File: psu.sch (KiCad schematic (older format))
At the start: 4 parts

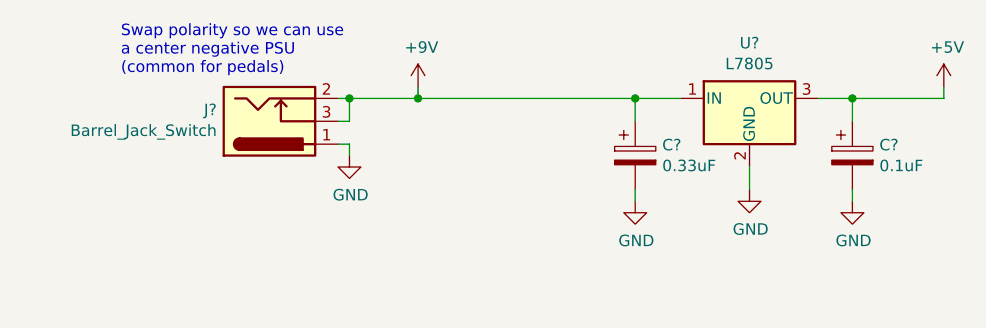
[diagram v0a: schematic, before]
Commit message: Schem entry done, need to do footprints and PCB
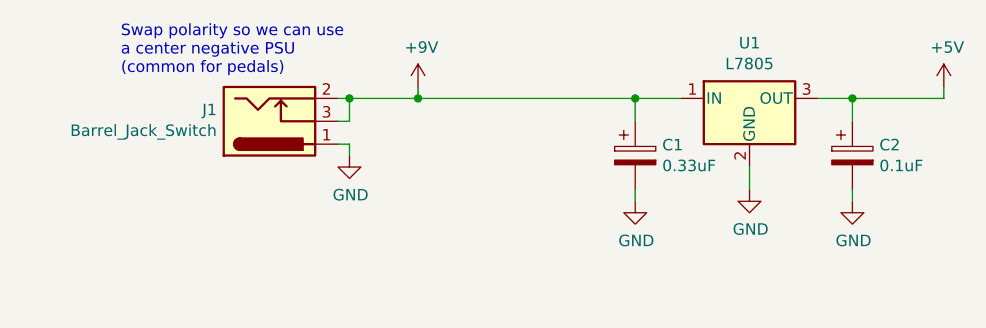
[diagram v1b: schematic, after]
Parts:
- gave numbers to parts that had none: 4
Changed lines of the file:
@@
 EESchema Schematic File Version 4
 LIBS:midi_switcher-cache
-EELAYER 29 0
+EELAYER 30 0
 EELAYER END
 $Descr A4 11693 8268
@@
 $EndDescr
 $Comp
-L Connector:Barrel_Jack_Switch J?
+L Connector:Barrel_Jack_Switch J1
 U 1 1 5D744931
 P 1550 1950
-F 0 "J?" H 1320 1900 50  0000 R CNN
+F 0 "J1" H 1320 1900 50  0000 R CNN
 F 1 "Barrel_Jack_Switch" H 1320 1991 50  0000 R CNN
 F 2 "" H 1600 1910 50  0001 C CNN
@@
 $EndComp
 $Comp
-L power:GND #PWR?
+L power:GND #PWR0101
 U 1 1 5D74594F
 P 1900 2100
-F 0 "#PWR?" H 1900 1850 50  0001 C CNN
+F 0 "#PWR0101" H 1900 1850 50  0001 C CNN
 F 1 "GND" H 1905 1927 50  0000 C CNN
 F 2 "" H 1900 2100 50  0001 C CNN
@@
 	1900 1850 2200 1850
 $Comp
-L power:+9V #PWR?
+L power:+9V #PWR0102
 U 1 1 5D7467A3
 P 2200 1800
-F 0 "#PWR?" H 2200 1650 50  0001 C CNN
+F 0 "#PWR0102" H 2200 1650 50  0001 C CNN
 F 1 "+9V" H 2215 1973 50  0000 C CNN
 F 2 "" H 2200 1800 50  0001 C CNN
@@
 $EndComp
 $Comp
-L Regulator_Linear:L7805 U?
+L Regulator_Linear:L7805 U1
 U 1 1 5D746EA6
 P 3650 1850
-F 0 "U?" H 3650 2092 50  0000 C CNN
+F 0 "U1" H 3650 2092 50  0000 C CNN
 F 1 "L7805" H 3650 2001 50  0000 C CNN
 F 2 "" H 3675 1700 50  0001 L CIN
@@
 $EndComp
 $Comp
-L power:GND #PWR?
+L power:GND #PWR0103
 U 1 1 5D747CA5
 P 3650 2250
-F 0 "#PWR?" H 3650 2000 50  0001 C CNN
+F 0 "#PWR0103" H 3650 2000 50  0001 C CNN
 F 1 "GND" H 3655 2077 50  0000 C CNN
 F 2 "" H 3650 2250 50  0001 C CNN
@@
 	3650 2250 3650 2150
 $Comp
-L Device:CP C?
+L Device:CP C1
 U 1 1 5D748082
 P 3150 2100
-F 0 "C?" H 3268 2146 50  0000 L CNN
+F 0 "C1" H 3268 2146 50  0000 L CNN
 F 1 "0.33uF" H 3268 2055 50  0000 L CNN
 F 2 "" H 3188 1950 50  0001 C CNN
@@
 $EndComp
 $Comp
-L Device:CP C?
+L Device:CP C2
 U 1 1 5D7482D3
 P 4100 2100
-F 0 "C?" H 4218 2146 50  0000 L CNN
+F 0 "C2" H 4218 2146 50  0000 L CNN
 F 1 "0.1uF" H 4218 2055 50  0000 L CNN
 F 2 "" H 4138 1950 50  0001 C CNN
@@
 $EndComp
 $Comp
-L power:GND #PWR?
+L power:GND #PWR0104
 U 1 1 5D7486E8
 P 3150 2300
-F 0 "#PWR?" H 3150 2050 50  0001 C CNN
+F 0 "#PWR0104" H 3150 2050 50  0001 C CNN
 F 1 "GND" H 3155 2127 50  0000 C CNN
 F 2 "" H 3150 2300 50  0001 C CNN
@@
 $EndComp
 $Comp
-L power:GND #PWR?
+L power:GND #PWR0105
 U 1 1 5D74897C
 P 4100 2300
-F 0 "#PWR?" H 4100 2050 50  0001 C CNN
+F 0 "#PWR0105" H 4100 2050 50  0001 C CNN
 F 1 "GND" H 4105 2127 50  0000 C CNN
 F 2 "" H 4100 2300 50  0001 C CNN
@@
 Connection ~ 4100 1850
 $Comp
-L power:+5V #PWR?
+L power:+5V #PWR0106
 U 1 1 5D74ADC8
 P 4500 1800
-F 0 "#PWR?" H 4500 1650 50  0001 C CNN
+F 0 "#PWR0106" H 4500 1650 50  0001 C CNN
 F 1 "+5V" H 4515 1973 50  0000 C CNN
 F 2 "" H 4500 1800 50  0001 C CNN

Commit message: pushing for work to do over holiday
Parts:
- added D6: 3MM Red LED, Connector_Wire:SolderWirePad_1x02_P3.81mm_Drill1mm, symbol Device:LED
- added R9: 400, Resistor_THT:R_Axial_DIN0207_L6.3mm_D2.5mm_P10.16mm_Horizontal, symbol Device:R
- C1: footprint (none) -> Capacitor_THT:CP_Radial_D5.0mm_P2.00mm
- C2: value 0.1uF -> 0.33uF; footprint (none) -> Capacitor_THT:CP_Radial_D5.0mm_P2.00mm
- J1: footprint (none) -> Connector_BarrelJack:BarrelJack_CUI_PJ-102AH_Horizontal
- U1: footprint (none) -> Package_TO_SOT_THT:TO-220-3_Vertical
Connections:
- net +9V: now also D6.2 (A)
- net GND: now also R9.2
- new net: D6.1 (K), R9.1
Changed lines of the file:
@@
 EESchema Schematic File Version 4
 LIBS:midi_switcher-cache
-EELAYER 30 0
+EELAYER 29 0
 EELAYER END
 $Descr A4 11693 8268
@@
 F 0 "J1" H 1320 1900 50  0000 R CNN
 F 1 "Barrel_Jack_Switch" H 1320 1991 50  0000 R CNN
-F 2 "" H 1600 1910 50  0001 C CNN
+F 2 "Connector_BarrelJack:BarrelJack_CUI_PJ-102AH_Horizontal" H 1600 1910 50  0001 C CNN
 F 3 "~" H 1600 1910 50  0001 C CNN
 	1    1550 1950
@@
 F 0 "U1" H 3650 2092 50  0000 C CNN
 F 1 "L7805" H 3650 2001 50  0000 C CNN
-F 2 "" H 3675 1700 50  0001 L CIN
+F 2 "Package_TO_SOT_THT:TO-220-3_Vertical" H 3675 1700 50  0001 L CIN
 F 3 "http://www.st.com/content/ccc/resource/technical/document/datasheet/41/4f/b3/b0/12/d4/47/88/CD00000444.pdf/files/CD00000444.pdf/jcr:content/translations/en.CD00000444.pdf" H 3650 1800 50  0001 C CNN
 	1    3650 1850
@@
 F 0 "C1" H 3268 2146 50  0000 L CNN
 F 1 "0.33uF" H 3268 2055 50  0000 L CNN
-F 2 "" H 3188 1950 50  0001 C CNN
+F 2 "Capacitor_THT:CP_Radial_D5.0mm_P2.00mm" H 3188 1950 50  0001 C CNN
 F 3 "~" H 3150 2100 50  0001 C CNN
 	1    3150 2100
@@
 P 4100 2100
 F 0 "C2" H 4218 2146 50  0000 L CNN
-F 1 "0.1uF" H 4218 2055 50  0000 L CNN
-F 2 "" H 4138 1950 50  0001 C CNN
+F 1 "0.33uF" H 4218 2055 50  0000 L CNN
+F 2 "Capacitor_THT:CP_Radial_D5.0mm_P2.00mm" H 4138 1950 50  0001 C CNN
 F 3 "~" H 4100 2100 50  0001 C CNN
 	1    4100 2100
@@
 	4100 1850 4100 1950
 Wire Wire Line
-	3150 1850 2200 1850
+	3150 1850 2600 1850
 Connection ~ 3150 1850
 Connection ~ 2200 1850
@@
 	1    0    0    -1
 $EndComp
+$Comp
+L Device:LED D6
+U 1 1 5DC759EC
+P 2600 2000
+F 0 "D6" V 2639 1883 50  0000 R CNN
+F 1 "3MM Red LED" V 2548 1883 50  0000 R CNN
+F 2 "Connector_Wire:SolderWirePad_1x02_P3.81mm_Drill1mm" H 2600 2000 50  0001 C CNN
+F 3 "~" H 2600 2000 50  0001 C CNN
+	1    2600 2000
+	0    -1   -1   0
+$EndComp
+Connection ~ 2600 1850
+Wire Wire Line
+	2600 1850 2200 1850
+$Comp
+L Device:R R9
+U 1 1 5DC76866
+P 2600 2350
+F 0 "R9" H 2670 2396 50  0000 L CNN
+F 1 "400" H 2670 2305 50  0000 L CNN
+F 2 "Resistor_THT:R_Axial_DIN0207_L6.3mm_D2.5mm_P10.16mm_Horizontal" V 2530 2350 50  0001 C CNN
+F 3 "~" H 2600 2350 50  0001 C CNN
+	1    2600 2350
+	1    0    0    -1
+$EndComp
+$Comp
+L power:GND #PWR0124
+U 1 1 5DC76C7C
+P 2600 2550
+F 0 "#PWR0124" H 2600 2300 50  0001 C CNN
+F 1 "GND" H 2605 2377 50  0000 C CNN
+F 2 "" H 2600 2550 50  0001 C CNN
+F 3 "" H 2600 2550 50  0001 C CNN
+	1    2600 2550
+	1    0    0    -1
+$EndComp
+Wire Wire Line
+	2600 2550 2600 2500
+Wire Wire Line
+	2600 2200 2600 2150
 $EndSCHEMATC
